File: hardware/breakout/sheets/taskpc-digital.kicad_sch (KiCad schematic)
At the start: 63 parts, among them J2 Connector 0 (analog + AISENSE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, J3 Connector 1 (digital, task PC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, J4 Manual reward button (panel), J5 Remote reward jack (parallel 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, J6 Reward driver out (BNC, place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, U10 SN74HCT541PW, U11 SN74HCT541PW, U12 SN74HCT32D, U13 SN74HCT14D, U5 SN74LVC541APW, U6 SN74LVC541APW, U7 SN74LVC541APW, U8 SN74HCT541PW, U9 SN74HCT541PW

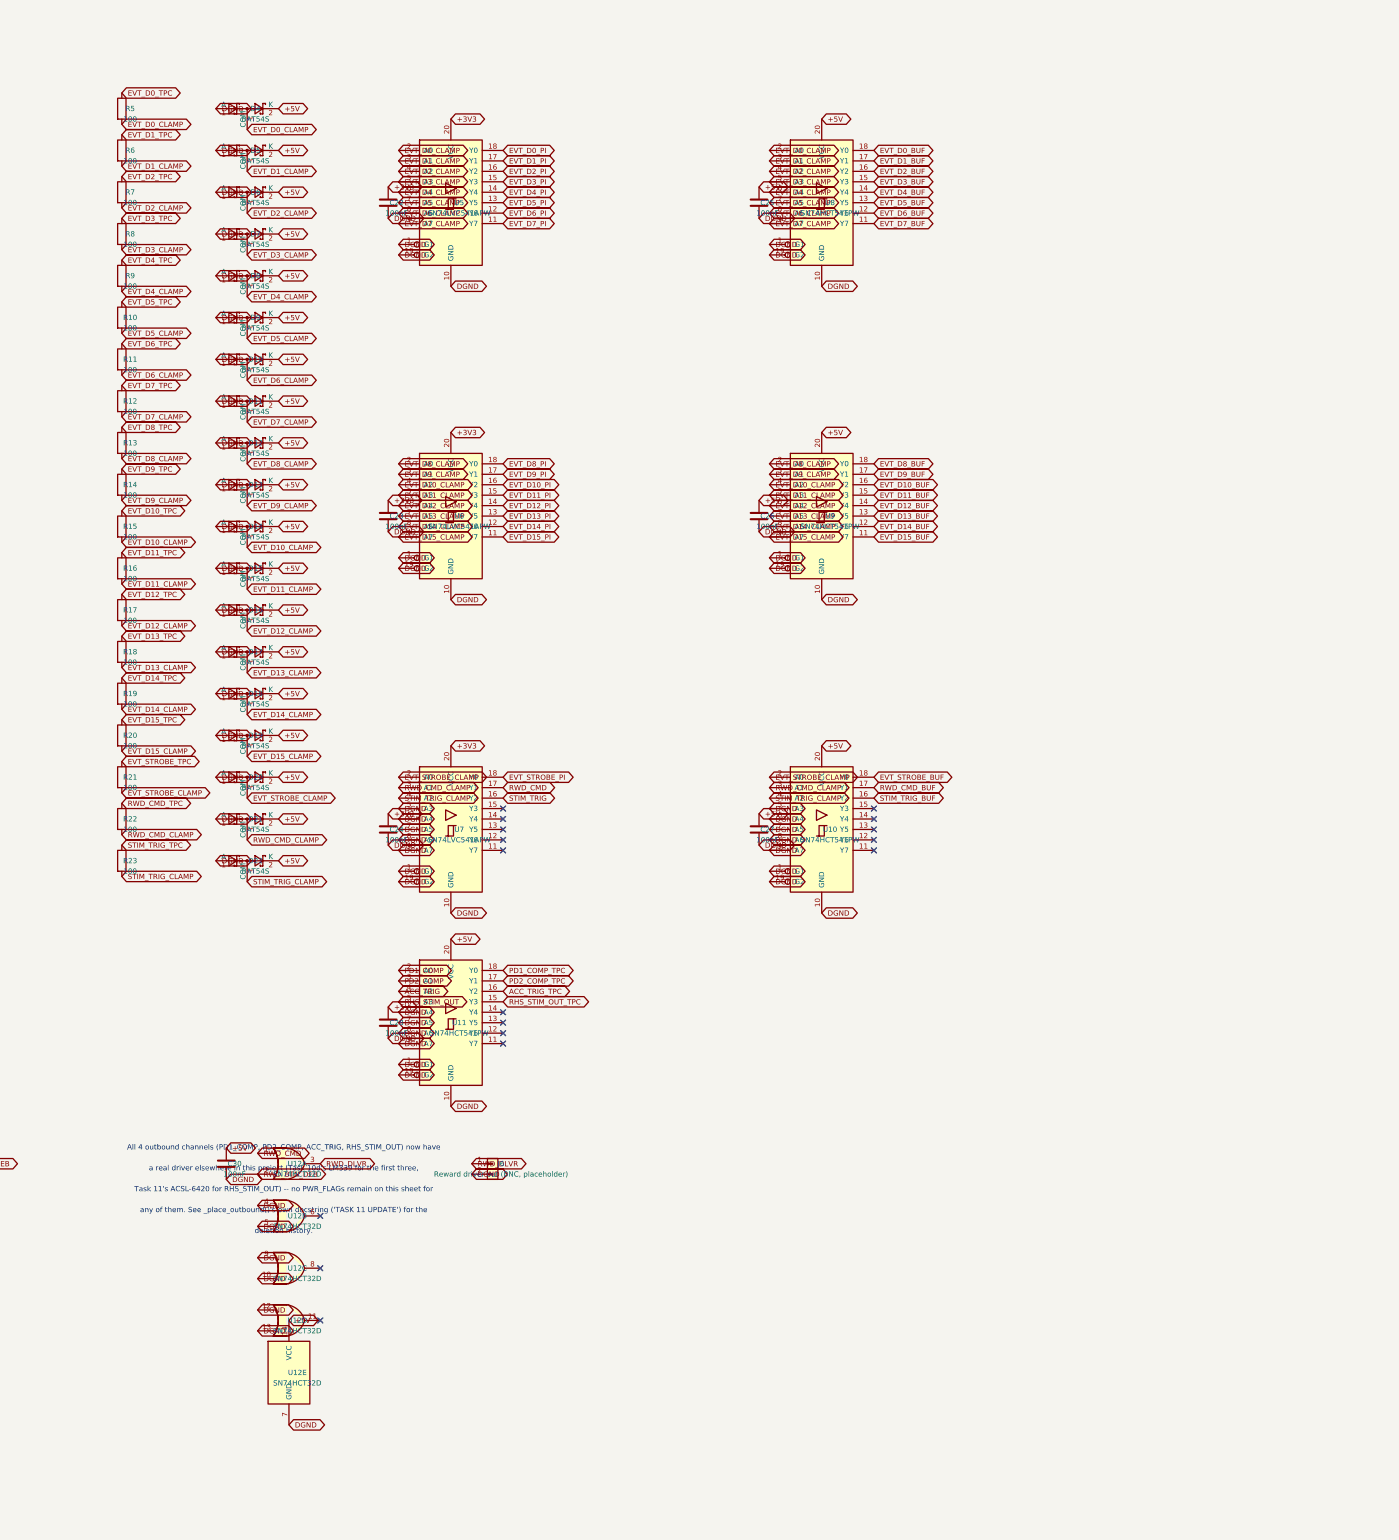
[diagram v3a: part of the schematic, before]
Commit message: fix(hw): one optocoupler LED per driver pin
The _BUF bank names 19 signals for what is really a 30-LED board. The 11
unnamed LEDs got doubled onto pins that already had one, and put +5V on
two sync-module GPIOs.

(a) Doubled loads. Each ACSL-6400/6420 LED draws ~7.33mA from +5V through
430R -- a value pinned between the part's 7-15mA recommended band and its
7.0mA worst-case switching threshold, so it cannot be lowered to suit a
driver. EVT_STROBE_BUF, RWD_CMD_BUF and STIM_TRIG_BUF each fed an NI LED
and an Intan LED from one HCT541 output (14.7mA vs 6mA IOL); BARCODE_PI
did the same off the pi-interface trigger buffer; and bare RWD_DLVR fed
both of its optocouplers straight off the 74HCT32 reward-OR gate, 14.7mA
against 4mA. That last one is the one with a failure mode rather than a
margin: RWD_DLVR's LOW is read by U14 (SN74LVC541APW, V_IL,max 0.8V), and
an HCT gate's VOL at 3.7x its rated sink plausibly exceeds it -- leaving
RWD_DLVR_PI stuck HIGH, the sync module recording reward-delivered
continuously. Same failure signature as the reward-OR polarity defect
caught on this board at task 8 fix round 1.

U10's 5 spare channels now carry EVT_STROBE_INTAN_BUF, RWD_CMD_INTAN_BUF,
STIM_TRIG_INTAN_BUF, RWD_DLVR_BUF and RWD_DLVR_INTAN_BUF (8 of 8 used);
U15's carry BARCODE_BUF and BARCODE_INTAN_BUF. The *_INTAN_BUF legs tap
the same *_CLAMP node their NI twin taps -- the established fan-out
point, one protection network with N buffered copies. RWD_DLVR and
BARCODE_PI now drive only CMOS inputs and panel headers.

(b) +5V reaching GPIO20/21 through an optocoupler LED. R166/R168 (430R
from +5V) fed ACSL-6400 LEDs whose cathodes sat on PD1_COMP/PD2_COMP --
which wire DIRECTLY into the sync module's GPIO20/21. With the LED off
that node idles ~3.6-3.8V, above the 3.3V rail and held only by the
module's ESD clamp; with this board powered and the sync box off, ~7mA is
injected into an unpowered pad. These were the only 2 of 24 NI
optocoupler LEDs not driven from a buffered le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
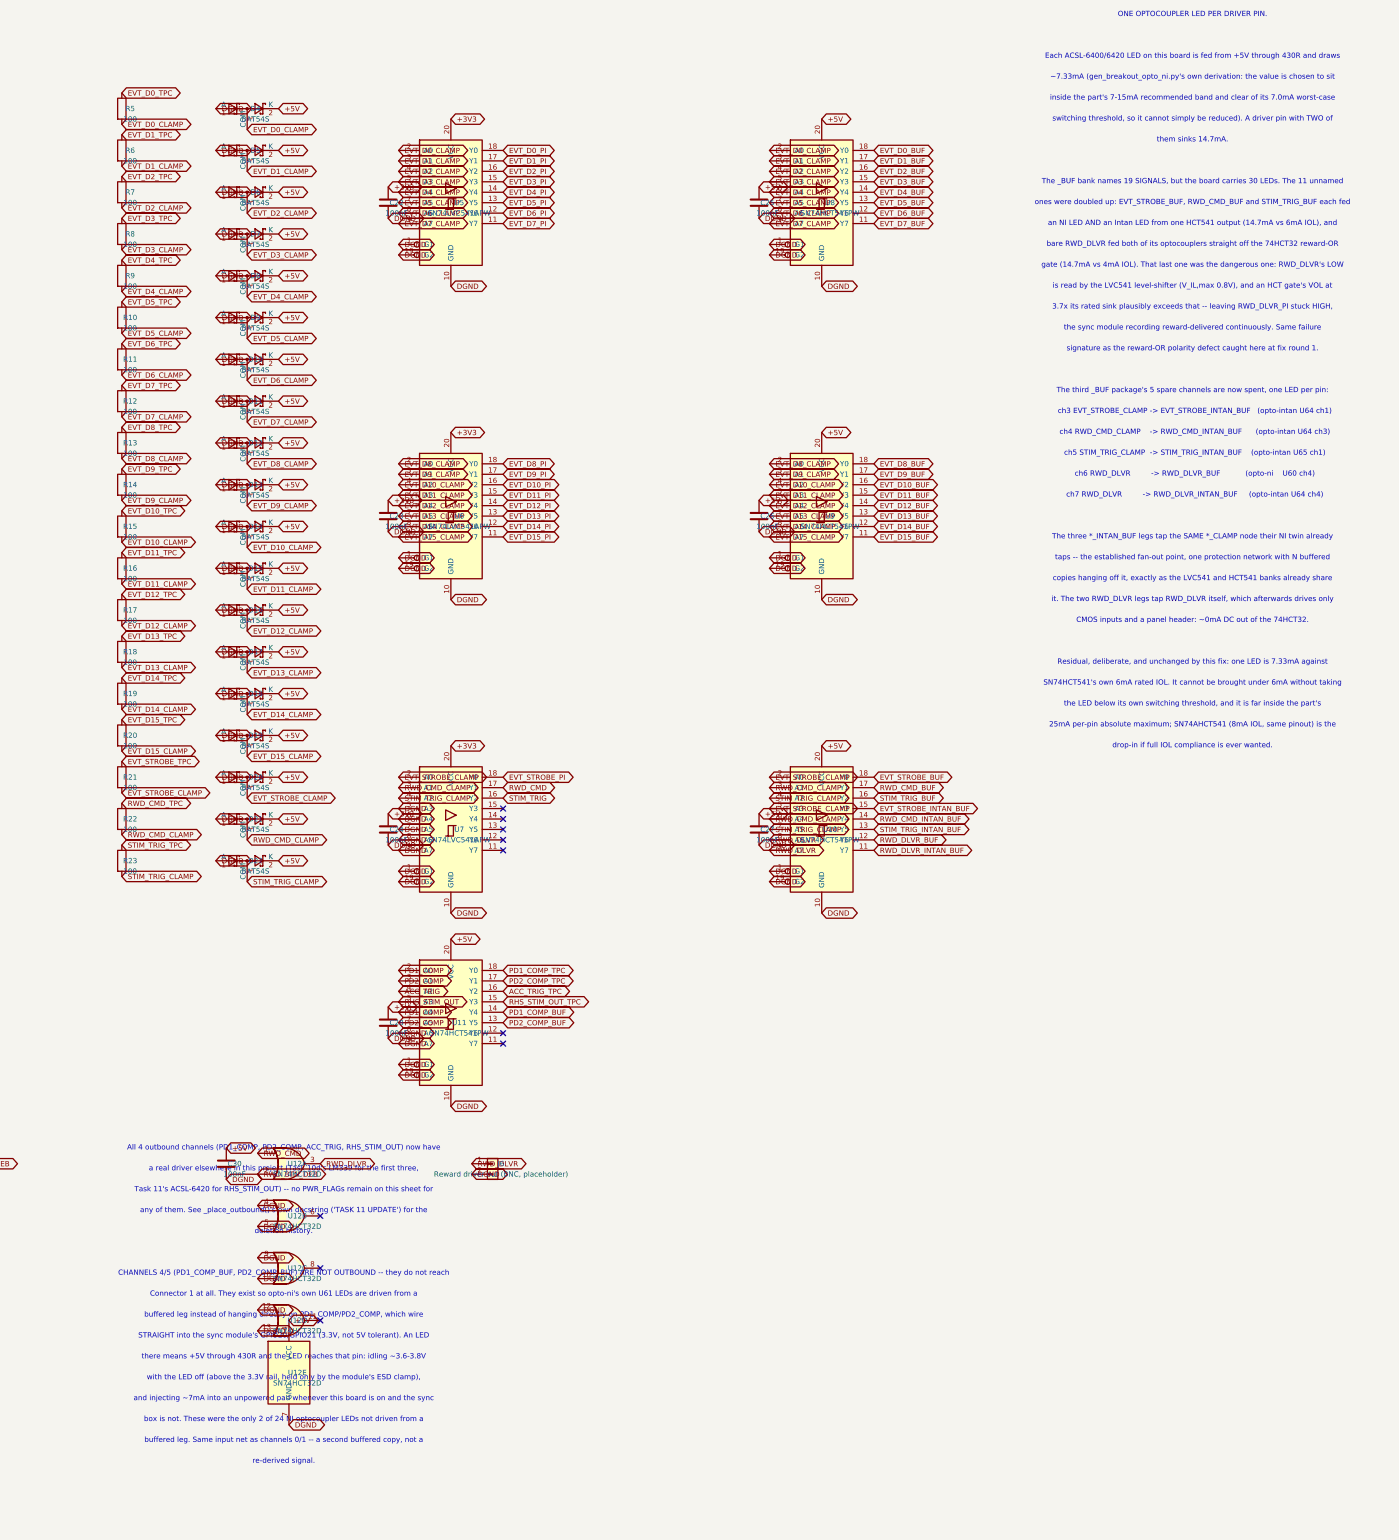
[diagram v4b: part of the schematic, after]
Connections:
- net DGND: no longer U10.5 (A3), U10.6 (A4), U10.7 (A5), U10.8 (A6), U10.9 (A7), U11.6 (A4), U11.7 (A5)
- net EVT_STROBE_CLAMP: now also U10.5 (A3)
- net PD1_COMP: now also U11.6 (A4)
- net PD2_COMP: now also U11.7 (A5)
- net RWD_CMD_CLAMP: now also U10.6 (A4)
- net RWD_DLVR: now also U10.8 (A6), U10.9 (A7)
- net STIM_TRIG_CLAMP: now also U10.7 (A5)
- net RWD_DLVR_INTAN_BUF: now reaches U10.11 (Y7)
- net RWD_DLVR_BUF: now reaches U10.12 (Y6)
- net STIM_TRIG_INTAN_BUF: now reaches U10.13 (Y5)
- net RWD_CMD_INTAN_BUF: now reaches U10.14 (Y4)
- net EVT_STROBE_INTAN_BUF: now reaches U10.15 (Y3)
- net PD2_COMP_BUF: now reaches U11.13 (Y5)
- net PD1_COMP_BUF: now reaches U11.14 (Y4)
- no-connect marks 113 -> 106
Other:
- note added: "25mA per-pin absolute maximum; SN74AHCT541 (8mA IOL, same pinout) is the"
- note added: "3.7x its rated sink plausibly exceeds that -- leaving RWD_DLVR_PI stuck HIGH,"
- note added: "CHANNELS 4/5 (PD1_COMP_BUF, PD2_COMP_BUF) ARE NOT OUTBOUND -- they do not reach"
- note added: "CMOS inputs and a panel header: ~0mA DC out of the 74HCT32."
- note added: "Connector 1 at all. They exist so opto-ni's own U61 LEDs are driven from a"
- note added: "Each ACSL-6400/6420 LED on this board is fed from +5V through 430R and draws"
- note added: "ONE OPTOCOUPLER LED PER DRIVER PIN."
- note added: "Residual, deliberate, and unchanged by this fix: one LED is 7.33mA against"
- note added: "SN74HCT541's own 6mA rated IOL. It cannot be brought under 6mA without taking"
- note added: "STRAIGHT into the sync module's GPIO20/GPIO21 (3.3V, not 5V tolerant). An LED"
- note added: "The _BUF bank names 19 SIGNALS, but the board carries 30 LEDs. The 11 unnamed"
- note added: "The third _BUF package's 5 spare channels are now spent, one LED per pin:"
- note added: "The three *_INTAN_BUF legs tap the SAME *_CLAMP node their NI twin already"
- note added: "an NI LED AND an Intan LED from one HCT541 output (14.7mA vs 6mA IOL), and"
- note added: "and injecting ~7mA into an unpowered pad whenever this board is on and the sync"
- note added: "bare RWD_DLVR fed both of its optocouplers straight off the 74HCT32 reward-OR"
- note added: "box is not. These were the only 2 of 24 NI optocoupler LEDs not driven from a"
- note added: "buffered leg instead of hanging directly on PD1_COMP/PD2_COMP, which wire"
- note added: "buffered leg. Same input net as channels 0/1 -- a second buffered copy, not a"
- note added: "ch3 EVT_STROBE_CLAMP -> EVT_STROBE_INTAN_BUF (opto-intan U64 ch1)"
- note added: "ch4 RWD_CMD_CLAMP -> RWD_CMD_INTAN_BUF (opto-intan U64 ch3)"
- note added: "ch5 STIM_TRIG_CLAMP -> STIM_TRIG_INTAN_BUF (opto-intan U65 ch1)"
- note added: "ch6 RWD_DLVR -> RWD_DLVR_BUF (opto-ni U60 ch4)"
- note added: "ch7 RWD_DLVR -> RWD_DLVR_INTAN_BUF (opto-intan U64 ch4)"
- note added: "copies hanging off it, exactly as the LVC541 and HCT541 banks already share"
- note added: "drop-in if full IOL compliance is ever wanted."
- note added: "gate (14.7mA vs 4mA IOL). That last one was the dangerous one: RWD_DLVR's LOW"
- note added: "inside the part's 7-15mA recommended band and clear of its 7.0mA worst-case"
- note added: "is read by the LVC541 level-shifter (V_IL,max 0.8V), and an HCT gate's VOL at"
- note added: "it. The two RWD_DLVR legs tap RWD_DLVR itself, which afterwards drives only"
- note added: "ones were doubled up: EVT_STROBE_BUF, RWD_CMD_BUF and STIM_TRIG_BUF each fed"
- note added: "re-derived signal."
- note added: "signature as the reward-OR polarity defect caught here at fix round 1."
- note added: "switching threshold, so it cannot simply be reduced). A driver pin with TWO of"
- note added: "taps -- the established fan-out point, one protection network with N buffered"
- note added: "the LED below its own switching threshold, and it is far inside the part's"
- note added: "the sync module recording reward-delivered continuously. Same failure"
- note added: "them sinks 14.7mA."
- note added: "there means +5V through 430R and the LED reaches that pin: idling ~3.6-3.8V"
- note added: "with the LED off (above the 3.3V rail, held only by the module's ESD clamp),"
- note added: "~7.33mA (gen_breakout_opto_ni.py's own derivation: the value is chosen to sit"
